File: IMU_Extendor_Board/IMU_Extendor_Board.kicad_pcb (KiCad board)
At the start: 2 copper layers, 54.9 x 55 mm, 79 parts, among them J101 USB_C_Receptacle_USB2.0_16P, J102 Conn_01x02_Pin, J201 DNP, J501 Conn_01x06_Pin, J601 Conn_01x07_Pin, J702 Conn_01x10_Pin, J703 Conn_01x04_Pin, U101 XC6210B332PR-G, U102 USBLC6-2SC6, U201 STM32F722RETx, U401 BNO086, U501 ICM-42688-P, Y202 Crystal, Y203 ECS-327KE, Y401 ECS-327KE, Y501 ECS-327KE

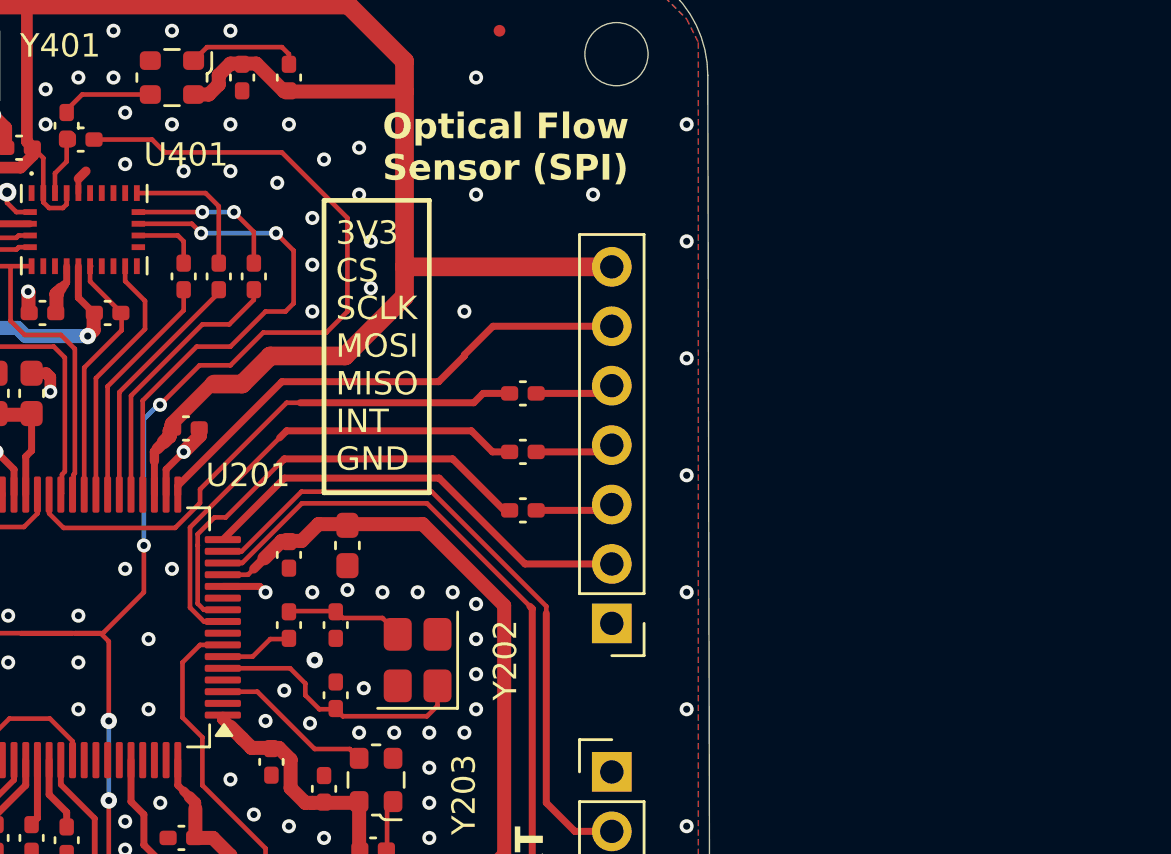
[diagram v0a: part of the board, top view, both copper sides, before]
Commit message: modifide the schematic to fix oscillator GND and in pcb; added ENV I2C pullpus in shematic
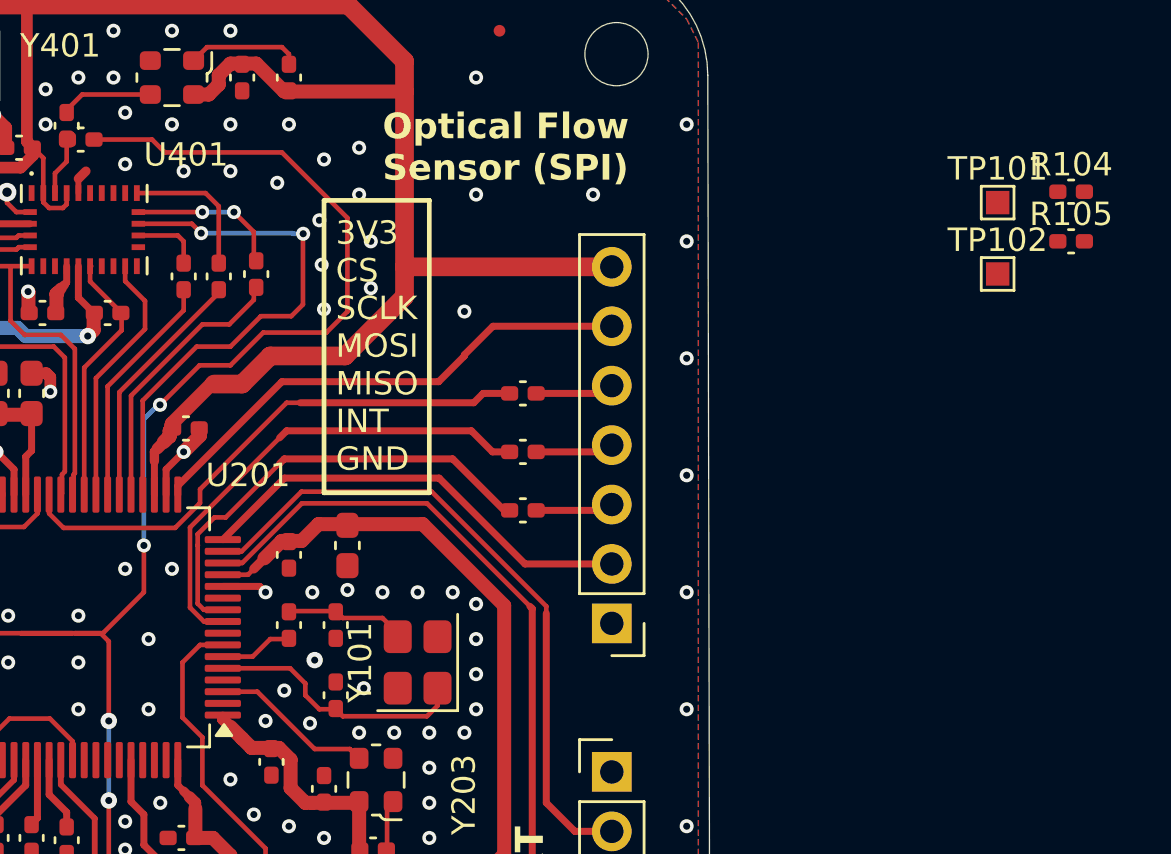
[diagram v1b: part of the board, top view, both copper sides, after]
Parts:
- removed Y202: Crystal, Crystal:Crystal_SMD_Abracon_ABM8G-4Pin_3.2x2.5mm
- added R104: 2k2, MYFootprints:0402_1005Metric_Pad0.74x0.62mm_HandSolder, F.Cu at (96.4, 36.9)
- added R105: 2k2, MYFootprints:0402_1005Metric_Pad0.74x0.62mm_HandSolder, F.Cu at (96.4, 39.0)
- added TP101: TestPoint, TestPoint:TestPoint_Pad_1.0x1.0mm, F.Cu at (93.3, 37.3)
- added TP102: TestPoint, TestPoint:TestPoint_Pad_1.0x1.0mm, F.Cu at (93.3, 40.4)
- added Y101: Crystal_GND24, Crystal:Crystal_SMD_Abracon_ABM8G-4Pin_3.2x2.5mm, F.Cu at (68.5, 57.0)
- moved R405 0.14 mm to (61.6, 40.4)
- renumbered R410 to R409, R409 to R410
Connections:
- U401 pad 15: unconnected-(U401-ENV_SCL-Pad15) -> /BNO_EVN_SCL
- U401 pad 16: unconnected-(U401-ENV_SDA-Pad16) -> /BNO_EVN_SDA
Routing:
- net BNO_CS1: track 21.6 -> 22.8 mm
